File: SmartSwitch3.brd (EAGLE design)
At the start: 100 x 50 mm, 24 parts

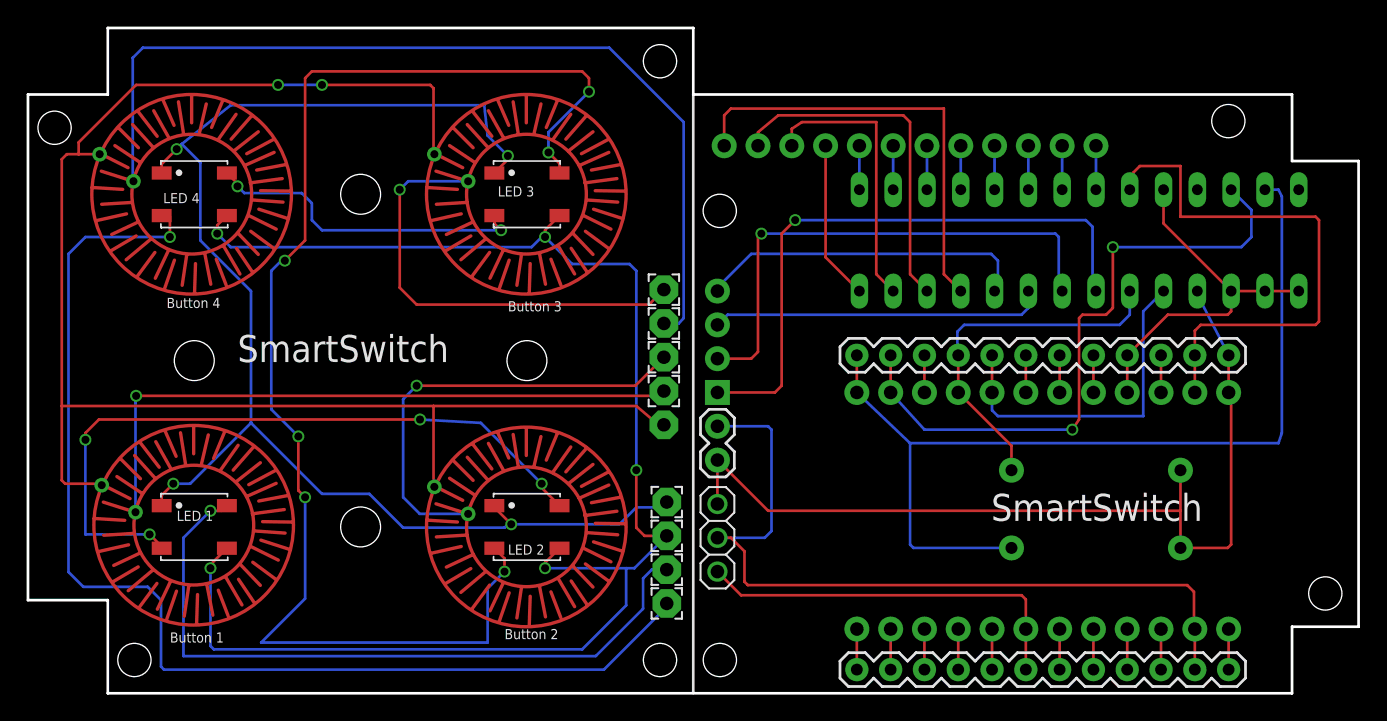
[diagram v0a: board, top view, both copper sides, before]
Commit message: series resistor, edges
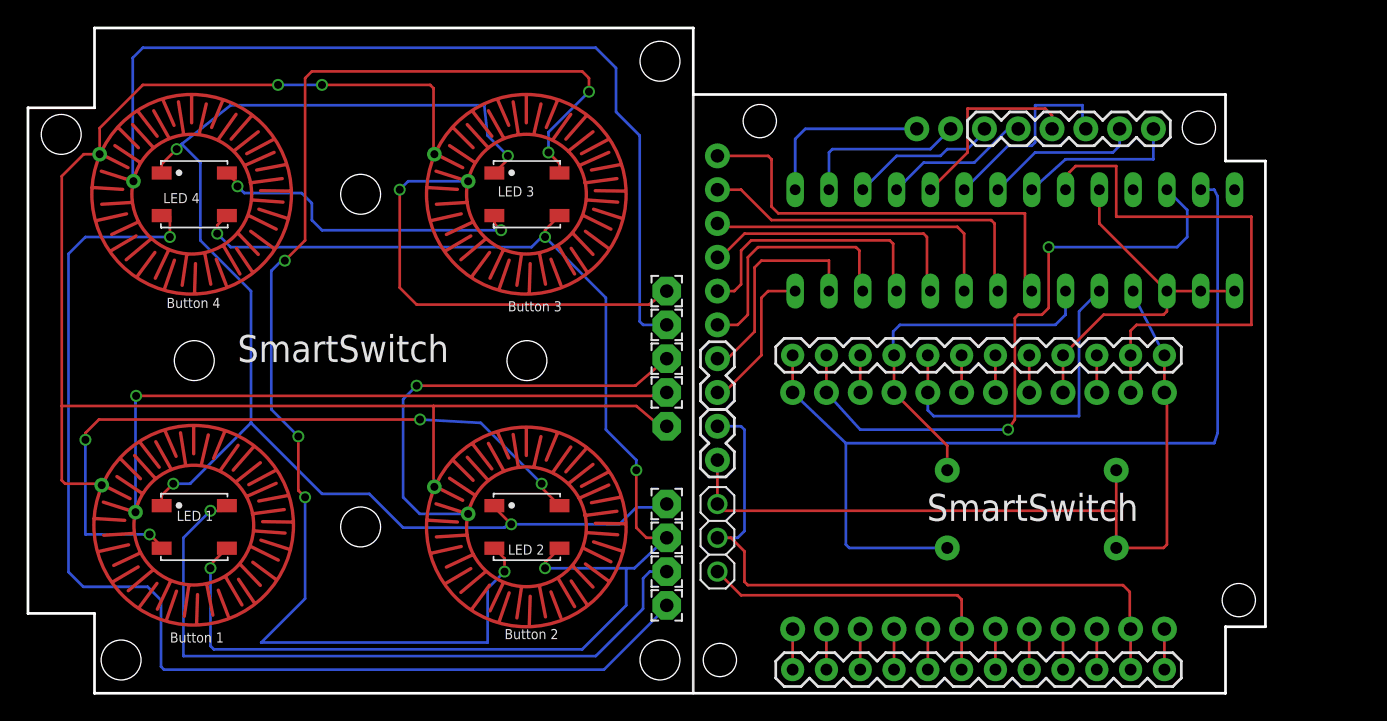
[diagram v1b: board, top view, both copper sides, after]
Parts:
- removed 5...16: (no value), SparkFun-Connectors:1X12
- added JP1: (no value), SparkFun-Connectors:1X06
- added JP3, JP7: M02PTH, SparkFun-Connectors:1X02
- BUTTONPAD: device SparkFun-Connectors:1X04 -> SparkFun-Connectors:1X06
- moved BUTTONPAD 17.8 mm to (51.8, 40.4), turned to 270 degrees
- moved JP4 4.83 mm to (57.5, 1.78)
- moved JP5 4.83 mm to (57.5, 25.4)
- moved MCP23017 4.83 mm to (74.2, 34.0)
- moved R1 4.83 mm to (75.4, 10.9)
- moved R2 4.83 mm to (75.4, 16.8)
- moved SPARK 4.83 mm to (71.4, 13.7)
- moved BTN2 0.24 mm to (48.0, 25.1)
- moved BTN3 0.24 mm to (48.0, 27.7)
- moved BTN4 0.24 mm to (48.0, 30.2)
- moved SWITCH 0.24 mm to (48.0, 20.1)
- moved BTN1 0.24 mm to (48.0, 22.6)
- moved GND 0.15 mm to (48.0, 11.7)
- moved OUT 0.15 mm to (48.0, 6.60)
- moved MOSI 0.15 mm to (48.0, 9.14)
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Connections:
- net N$14: now also BUTTONPAD.5; no longer 5...16.1
- net N$15: now also BUTTONPAD.6; no longer 5...16.2
- net N$16: now also JP7.1; no longer 5...16.3
- net N$17: now also JP7.2; no longer 5...16.4
- net N$18: now also JP3.1; no longer 5...16.5
- net N$19: now also JP3.2; no longer 5...16.6
- net N$20: now also JP1.1; no longer 5...16.7
- net N$21: now also JP1.2; no longer 5...16.8
- net N$22: now also JP1.3; no longer 5...16.9
- net N$23: now also JP1.4; no longer 5...16.10
- net N$24: now also JP1.5; no longer 5...16.11
- net N$25: now also JP1.6; no longer 5...16.12
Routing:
- net N$14: track 33.2 -> 20.0 mm
- net N$5: track 45.4 -> 33.0 mm, vias 1 -> 0
- net N$6: track 38.9 -> 27.1 mm, vias 1 -> 0
- net N$23: track 3.30 -> 15.0 mm
- net N$22: track 3.30 -> 14.8 mm
- net N$18: track 3.30 -> 13.3 mm
- net N$19: track 3.30 -> 12.7 mm
- net N$25: track 3.30 -> 12.3 mm
- net N$30: track 60.8 -> 51.9 mm
- net N$24: track 3.30 -> 11.8 mm
- net N$20: track 3.30 -> 11.2 mm
- net N$21: track 3.30 -> 11.0 mm
- net N$15: track 26.3 -> 18.9 mm
- net N$28: track 69.1 -> 63.1 mm
- net N$29: track 29.3 -> 24.5 mm
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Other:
- board size 100 x 50 mm -> 93 x 50 mm

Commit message: Change Jumper
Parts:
- removed LEDS: (no value), adafruit:1X03
- added JP6: (no value), SparkFun-Connectors:1X03
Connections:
- net N$28: now also JP6.3; no longer LEDS.1
- net N$29: now also JP6.1; no longer LEDS.3
- net N$30: now also JP6.2; no longer LEDS.2
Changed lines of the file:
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@@
 <attribute name="VALUE" x="58.42" y="34.9758" size="1.778" layer="28" ratio="10" rot="MR180"/>
-</element>
-<element name="LEDS" library="adafruit" package="1X03" value="" x="51.816" y="11.684" smashed="yes" rot="R270">
-<attribute name="VALUE" x="48.641" y="15.494" size="1.27" layer="27" rot="R270"/>
 </element>
 <element name="R1" library="SparkFun-Passives" package="AXIAL-0.5" value="" x="75.438" y="10.922" smashed="yes" rot="SMR0">
@@
 <attribute name="VALUE" x="78.867" y="16.383" size="0.8128" layer="22" font="vector" ratio="15" rot="SMR0"/>
 </element>
-<element name="BUTTONPAD" library="SparkFun-Connectors" package="1X06" value="" x="51.816" y="40.386" smashed="yes" rot="MR270">
-<attribute name="VALUE" x="49.911" y="41.656" size="1.27" layer="28" rot="MR270"/>
-<attribute name="PROD_ID" value="CONN-08437" x="51.816" y="40.386" size="1.778" layer="28" rot="MR270" display="off"/>
+<element name="BUTTONPAD" library="SparkFun-Connectors" package="1X06" value="" x="51.816" y="40.386" smashed="yes" rot="SMR270">
+<attribute name="VALUE" x="49.911" y="41.656" size="1.27" layer="28" rot="SMR270"/>
+<attribute name="PROD_ID" value="CONN-08437" x="51.816" y="40.386" size="1.778" layer="28" rot="SMR270" display="off"/>
 </element>
 <element name="SPARK" library="Spark" package="SPARK_CORE" value="SPARK_CORECORE" x="71.438" y="13.716" smashed="yes" rot="MR90">
@@
 <attribute name="VALUE" x="48.006" y="19.066" size="0.0254" layer="28" rot="MR180"/>
 </element>
-<element name="JP2" library="SparkFun-Connectors" package="1X02" value="M02PTH" x="51.816" y="20.066" smashed="yes" rot="R270"/>
-<element name="JP1" library="SparkFun-Connectors" package="1X06" value="" x="71.882" y="42.418" smashed="yes">
-<attribute name="PROD_ID" value="CONN-08437" x="71.882" y="42.418" size="1.778" layer="27" display="off"/>
-<attribute name="VALUE" x="70.612" y="39.243" size="1.27" layer="27"/>
-</element>
-<element name="JP3" library="SparkFun-Connectors" package="1X02" value="M02PTH" x="66.802" y="42.418" smashed="yes" rot="MR180"/>
+<element name="JP2" library="SparkFun-Connectors" package="1X02" value="M02PTH" x="51.816" y="20.066" smashed="yes" rot="SR270"/>
+<element name="JP1" library="SparkFun-Connectors" package="1X06" value="" x="71.882" y="42.418" smashed="yes" rot="SR0">
+<attribute name="PROD_ID" value="CONN-08437" x="71.882" y="42.418" size="1.778" layer="27" rot="SR0" display="off"/>
+<attribute name="VALUE" x="70.612" y="39.243" size="1.27" layer="27" rot="SR0"/>
+</element>
+<element name="JP3" library="SparkFun-Connectors" package="1X02" value="M02PTH" x="66.802" y="42.418" smashed="yes" rot="SMR180"/>
 <element name="JP7" library="SparkFun-Connectors" package="1X02" value="M02PTH" x="51.816" y="25.146" smashed="yes" rot="R270"/>
+<element name="JP6" library="SparkFun-Connectors" package="1X03" value="" x="51.816" y="9.144" smashed="yes" rot="SR90">
+<attribute name="VALUE" x="54.991" y="7.874" size="1.27" layer="27" rot="SR90"/>
+</element>
 </elements>
 <signals>
@@
 <contactref element="JP5" pad="12"/>
 <contactref element="JP2" pad="2"/>
-<contactref element="LEDS" pad="1"/>
 <wire x1="85.408" y1="25.4" x2="83.058" y2="29.972" width="0.2032" layer="16"/>
 <wire x1="83.058" y1="29.972" x2="83.058" y2="30.226" width="0.2032" layer="16"/>
@@
 <wire x1="52.07" y1="13.716" x2="81.788" y2="13.716" width="0.2032" layer="1"/>
 <wire x1="52.07" y1="13.716" x2="51.816" y2="13.97" width="0.2032" layer="1"/>
+<contactref element="JP6" pad="3"/>
 <wire x1="51.816" y1="13.97" x2="51.816" y2="14.224" width="0.2032" layer="1"/>
 <wire x1="51.816" y1="17.526" x2="51.816" y2="14.224" width="0.2032" layer="1"/>
 </signal>
 <signal name="N$29">
-<contactref element="LEDS" pad="3"/>
 <contactref element="SPARK" pad="7"/>
 <contactref element="JP4" pad="6"/>
 <wire x1="70.168" y1="4.826" x2="70.168" y2="1.778" width="0.2032" layer="1"/>
-<wire x1="51.816" y1="9.144" x2="53.594" y2="7.366" width="0.2032" layer="1"/>
 <wire x1="53.594" y1="7.366" x2="69.85" y2="7.366" width="0.2032" layer="1"/>
 <wire x1="69.85" y1="7.366" x2="70.168" y2="7.048" width="0.2032" layer="1"/>
 <wire x1="70.168" y1="7.048" x2="70.168" y2="4.826" width="0.2032" layer="1"/>
+<contactref element="JP6" pad="1"/>
+<wire x1="53.594" y1="7.366" x2="51.816" y2="9.144" width="0.2032" layer="1"/>
 </signal>
 <signal name="N$30">
-<contactref element="LEDS" pad="2"/>
 <contactref element="SPARK" pad="2"/>
 <contactref element="JP4" pad="11"/>
 <wire x1="82.868" y1="4.826" x2="82.868" y2="1.778" width="0.2032" layer="1"/>
 <contactref element="JP2" pad="1"/>
-<wire x1="51.816" y1="11.684" x2="53.34" y2="11.684" width="0.2032" layer="16"/>
 <wire x1="53.34" y1="11.684" x2="53.848" y2="12.192" width="0.2032" layer="16"/>
 <wire x1="53.848" y1="12.192" x2="53.848" y2="19.812" width="0.2032" layer="16"/>
@@
 <wire x1="53.848" y1="8.382" x2="53.848" y2="10.668" width="0.2032" layer="1"/>
 <wire x1="53.848" y1="10.668" x2="52.832" y2="11.684" width="0.2032" layer="1"/>
+<contactref element="JP6" pad="2"/>
 <wire x1="52.832" y1="11.684" x2="51.816" y2="11.684" width="0.2032" layer="1"/>
+<wire x1="53.34" y1="11.684" x2="51.816" y2="11.684" width="0.2032" layer="16"/>
 </signal>
 <signal name="N$32">
